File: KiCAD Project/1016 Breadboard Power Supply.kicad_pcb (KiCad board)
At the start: 2 copper layers, 52.3 x 52.8 mm, 80 parts, among them J1 PJ-102B, J2 TC2030-IDC, J3 Pin Hdr 2x2, J4 Pin Hdr 2x2, P1 DW_PCB_Logo, P2 Solder_Stencil_Alignment_Pin, P3 Solder_Stencil_Alignment_Pin, Q1 BUK6D120-60PX, U1 TPS62130RGTR, U2 TPS62130RGTR, U3 TPS62130RGTR, U4 STM32C011F4U6TR

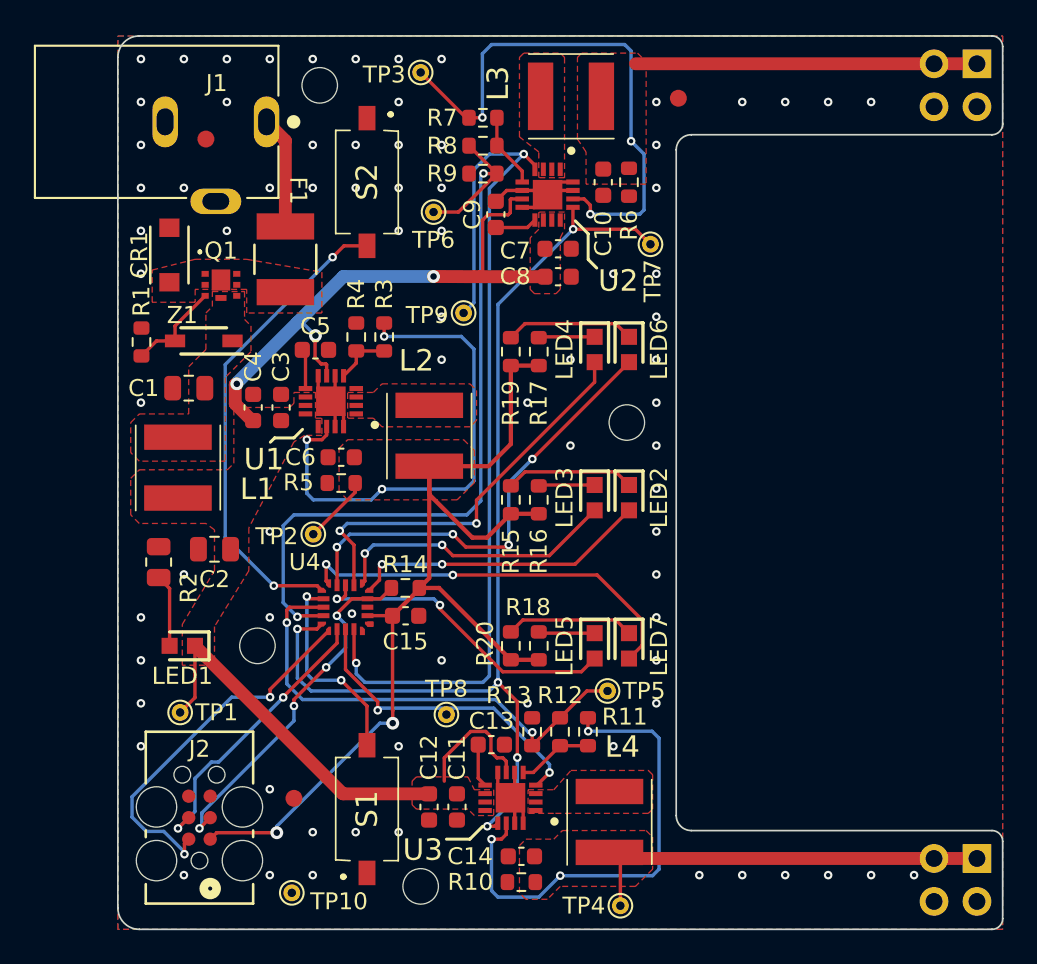
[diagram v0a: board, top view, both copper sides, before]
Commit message: v2.0.0.0
1016 Breadboard Power Supply v2

- Change FSW connection to the Vout on all regulators
- Change regulator to TPS62130A so that PG pin goes low on thermal shutdown and UVLO
- Change PG pullup to be a resistor at the regulator vice pullup within STM32 so that it can be actively discharged
- Remove resistor across rail outputs for discharging to improve efficiency
- Change board dimensions to correct span
- Change pinout of STM32 for better routing
- Change Tag-Connect footprint to momentary connection (no legs)
- Make sure Tag-Connect footprint doesn't have solder paste layer
- Added heat sinks on bottom under rail regulators, added thermal vias
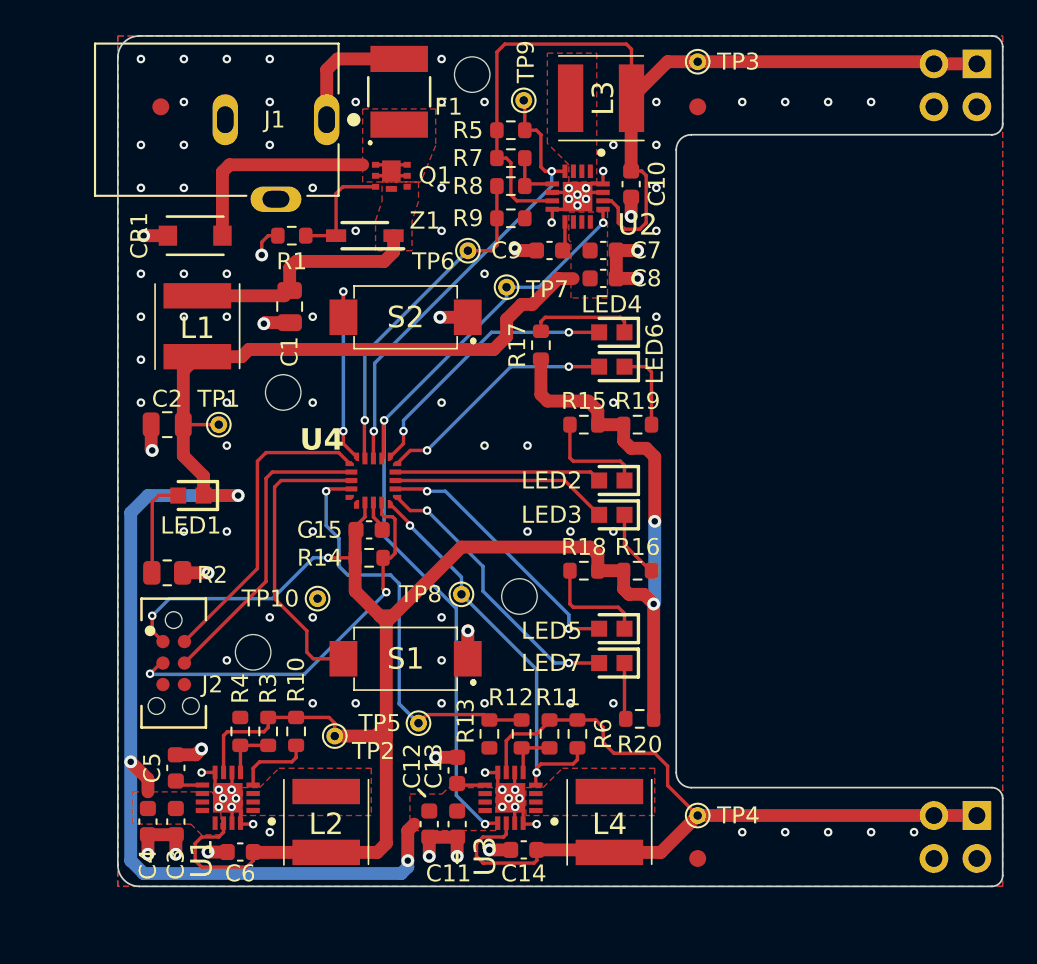
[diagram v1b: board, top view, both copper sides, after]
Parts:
- added HS1: Heat Sink, 1016:HSB01-080808, B.Cu at (71.5, 116.4)
- added HS2: Heat Sink, 1016:HSB01-080808, B.Cu at (75.5, 80.9)
- J2: value TC2030-IDC -> TC2030-IDC-NL; footprint 1016:CONN_TC2030-IDC_TGC -> 1016:CONN_TC2030-IDC-NL_TGC
- R10, R5, R6: value 1K6 -> 10K
- U1, U2, U3: value TPS62130RGTR -> TPS62130ARGTR
- moved R6 32.8 mm to (75.4, 112.6), turned to -90 degrees
- moved FID1 30.6 mm to (50.8, 75.6)
- moved H3 30.3 mm to (58.0, 92.5)
- moved FID2 29.1 mm to (82.5, 75.6)
- moved P1 28.0 mm to (66.7, 105.2)
- moved C5 26.1 mm to (51.7, 114.7), turned to -90 degrees
- moved H2 25.9 mm to (56.3, 107.8)
- moved C3 25.3 mm to (51.7, 117.8), turned to -90 degrees
- moved C4 25.3 mm to (50.0, 117.8), turned to -90 degrees
- moved R3 24.3 mm to (57.1, 112.5)
- moved R4 24.3 mm to (55.5, 112.5)
- moved U1 24.2 mm to (54.8, 116.4)
- moved FID3 24.1 mm to (82.5, 120.0)
- moved C6 24.1 mm to (55.5, 119.6)
- moved L2 23.6 mm to (60.6, 117.9)
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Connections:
- R10 pad 1: /Input Power/GND -> /MCU Power Regulator/PGood_MCU
- R10 pad 2: /Rail B Power Regulator/VrailB -> /MCU Control/Vmcu
- R5 pad 1: /Input Power/GND -> /Rail Output/VrailT
- R5 pad 2: /MCU Control/Vmcu -> /MCU Control/PGood_RailT
- R6 pad 1: /Input Power/GND -> /Rail B Power Regulator/VrailB
- R6 pad 2: /Rail Output/VrailT -> /MCU Control/PGood_RailB
- U1 pad 4: unconnected-(U1-PG-Pad4) -> /MCU Power Regulator/PGood_MCU
- U1 pad 7: /Input Power/VCC -> /MCU Control/Vmcu
- U2 pad 7: /Input Power/VCC -> /Rail Output/VrailT
- U3 pad 7: /Input Power/VCC -> /Rail B Power Regulator/VrailB
- U4 pad 10: /MCU Control/3V3BLED_Sig -> /MCU Control/3V3TLED_Sig
- U4 pad 11: /MCU Control/Btn_Config -> /MCU Control/5VTLED_Sig
- U4 pad 12: /MCU Control/Btn_OutputEn -> /MCU Control/Enable_Output
- U4 pad 13: /MCU Control/SelectVrailB -> /MCU Control/PGood_RailT
- U4 pad 15: /MCU Control/Enable_Output -> /MCU Control/Btn_Config
- U4 pad 18: /MCU Control/PGood_RailB -> /MCU Control/Btn_OutputEn
- U4 pad 19: /MCU Control/PGood_RailT -> /MCU Control/SelectVrailB
- U4 pad 5: /MCU Control/ErrorLED_Sig -> /MCU Control/PGood_RailB
- U4 pad 6: /MCU Control/OutputLED_Sig -> /MCU Control/3V3BLED_Sig
- U4 pad 7: /MCU Control/5VTLED_Sig -> /MCU Control/5VBLED_Sig
- U4 pad 8: /MCU Control/5VBLED_Sig -> /MCU Control/OutputLED_Sig
- U4 pad 9: /MCU Control/3V3TLED_Sig -> /MCU Control/ErrorLED_Sig
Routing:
- net /Input Power/GND: track 22.3 -> 52.6 mm, vias 78 -> 112
- net /MCU Control/PGood_RailT: track 55.9 -> 27.6 mm
- net /MCU Control/SelectVrailT: track 46.8 -> 20.2 mm, vias 2 -> 1
- net /Input Power/VCC: track 63.9 -> 87.0 mm
- net /MCU Control/Vmcu: track 95.4 -> 115.3 mm, vias 5 -> 4
- net /MCU Control/Btn_Config: track 28.5 -> 11.6 mm
- net /Input Power/Vfused: track 0.00 -> 16.5 mm
- net /Input Power/Vprot: track 0.00 -> 14.4 mm
- net /MCU Control/Enable_Output: track 61.9 -> 48.4 mm, vias 5 -> 3
- net /MCU Control/3V3TLED_Sig: track 26.8 -> 14.3 mm, vias 4 -> 2
- net /MCU Control/5VTLED_Sig: track 24.3 -> 16.2 mm
- net /MCU Control/3V3BLED_Sig: track 23.9 -> 16.9 mm
- net /MCU Control/ErrorLED_Sig: track 17.8 -> 12.3 mm, vias 2 -> 0
- net /MCU Control/Btn_OutputEn: track 12.3 -> 17.6 mm, vias 2 -> 0
- net /MCU Control/PGood_RailB: track 18.8 -> 23.8 mm
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- removed copper zone on F.Cu, net /MCU Control/Vmcu
- removed copper zone on F.Cu, net /Rail B Power Regulator/VrailB
- removed copper zone on F.Cu, net /Rail Output/VrailT
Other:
- board size 52.3 x 52.8 mm -> 52.3 x 50.3 mm
